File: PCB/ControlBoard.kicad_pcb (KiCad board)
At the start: 2 copper layers, 15 parts, among them J1 Conn_01x02, J2 Conn_01x12, SW1 SW_Push, SW2 SW_Push, SW3 SW_Push, U1 Nokia_5510_display_module

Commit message: Board done
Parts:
- added C2: 100u, Capacitor_SMD:C_0603_1608Metric_Pad1.08x0.95mm_HandSolder, B.Cu at (101.5, 110.5)
- added C3: 100u, Capacitor_SMD:C_0603_1608Metric_Pad1.08x0.95mm_HandSolder, B.Cu at (78.0, 90.8)
- added J3: Conn_01x13, Connector_PinHeader_2.54mm:PinHeader_1x13_P2.54mm_Vertical, F.Cu at (80.3, 75.2)
- added R9: 10k, Resistor_SMD:R_0402_1005Metric_Pad0.72x0.64mm_HandSolder, B.Cu at (88.0, 107.0)
- added REF**: MountingHole_3mm_Pad_TopOnly, MountingHole:MountingHole_3mm_Pad_TopOnly, F.Cu at (74.8, 108.8)
- added REF**: MountingHole_3mm_Pad_TopOnly, MountingHole:MountingHole_3mm_Pad_TopOnly, F.Cu at (74.8, 70.0)
- added REF**: MountingHole_3mm_Pad_TopOnly, MountingHole:MountingHole_3mm_Pad_TopOnly, F.Cu at (152.0, 108.8)
- added REF**: MountingHole_3mm_Pad_TopOnly, MountingHole:MountingHole_3mm_Pad_TopOnly, F.Cu at (152.0, 70.2)
- C1, R1, R2, R3, R4, R5, R6, R7, R8: moved to B.Cu
- J2: value Conn_01x12 -> Conn_01x02; footprint Connector_PinHeader_2.54mm:PinHeader_1x12_P2.54mm_Vertical -> Connector_PinHeader_2.54mm:PinHeader_1x02_P2.54mm_Horizontal
- moved J2 72.4 mm to (150.9, 95.0)
- moved J1 24.2 mm to (151.1, 77.7), turned to 0 degrees
- moved R1 15.8 mm to (148.0, 77.0)
- moved C1 15.7 mm to (147.0, 81.0), turned to 180 degrees
- moved R8 7.52 mm to (86.5, 87.9), turned to 180 degrees
- moved R2 5.34 mm to (96.3, 85.3)
- moved SW1 1.37 mm to (143.0, 71.1)
- moved SW3 0.80 mm to (142.7, 100.1)
- moved R5 0.57 mm to (93.5, 77.7), turned to 180 degrees
- moved SW2 0.57 mm to (143.0, 84.8)
- moved R3 0.25 mm to (90.2, 82.8)
- moved R6 0.25 mm to (90.2, 90.4)
- moved R4 0.25 mm to (96.5, 80.3)
- moved R7 0.25 mm to (91.4, 75.2)
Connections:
- J2 pad 1: RST -> GND
- J2 pad 2: CE -> REL
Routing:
- net +5V: track 0.00 -> 104.0 mm
- net THERM: track 0.00 -> 102.9 mm, vias 0 -> 2
- net REL: track 0.00 -> 83.9 mm, vias 0 -> 2
- net BTN1: track 0.00 -> 72.1 mm, vias 0 -> 2
- net BTN2: track 0.00 -> 67.6 mm, vias 0 -> 2
- net BTN3: track 0.00 -> 64.7 mm, vias 0 -> 2
- net Net-(R7-Pad2): track 0.00 -> 48.9 mm
- net Net-(R5-Pad1): track 0.00 -> 41.9 mm
- net Net-(R3-Pad2): track 0.00 -> 37.6 mm
- net Net-(R4-Pad2): track 0.00 -> 35.4 mm
- net +3V3: track 0.00 -> 32.7 mm
- net Net-(R2-Pad2): track 0.00 -> 26.6 mm
- net Net-(R6-Pad2): track 0.00 -> 22.7 mm
- net DC: track 0.00 -> 15.9 mm
- net CLK: track 0.00 -> 15.7 mm
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- added copper zone on B.Cu, net GND
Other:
- board outline added: 84 x 45.2 mm
- rule trace_min: 0.2 -> 0.5

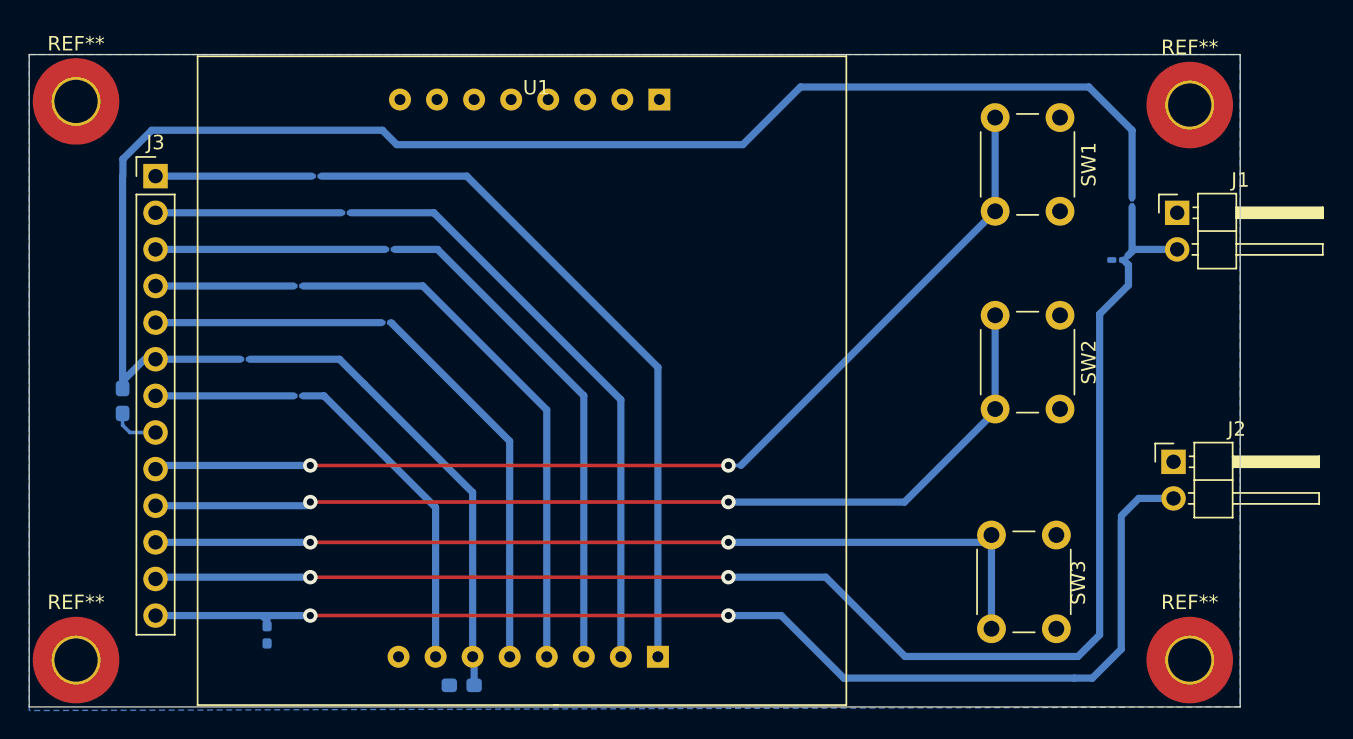
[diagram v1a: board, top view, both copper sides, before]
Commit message: Fixed some holes and footprints so I can mill this at home
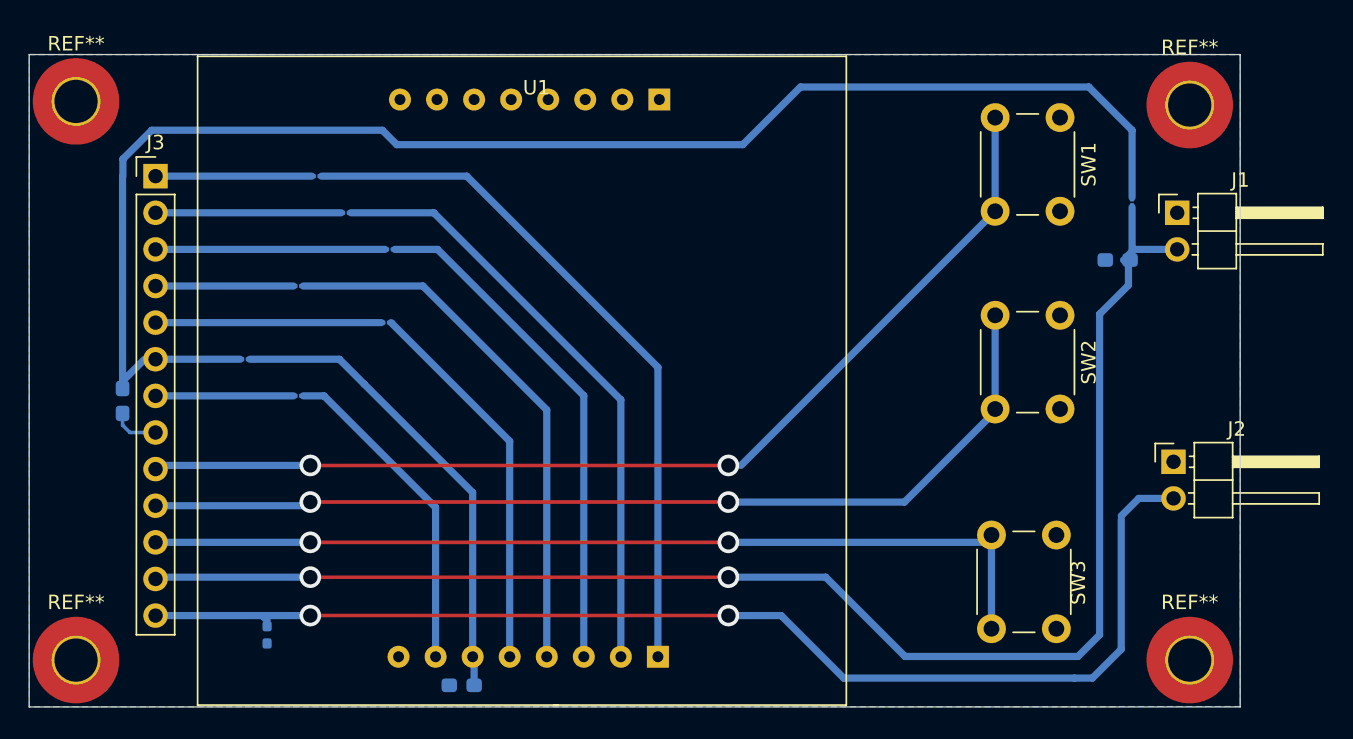
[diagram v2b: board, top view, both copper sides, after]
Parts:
- C1: footprint Capacitor_SMD:C_0201_0603Metric_Pad0.64x0.40mm_HandSolder -> Capacitor_SMD:C_0603_1608Metric_Pad1.08x0.95mm_HandSolder
